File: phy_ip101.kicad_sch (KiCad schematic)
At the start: 48 parts, among them U4 IP101GRI

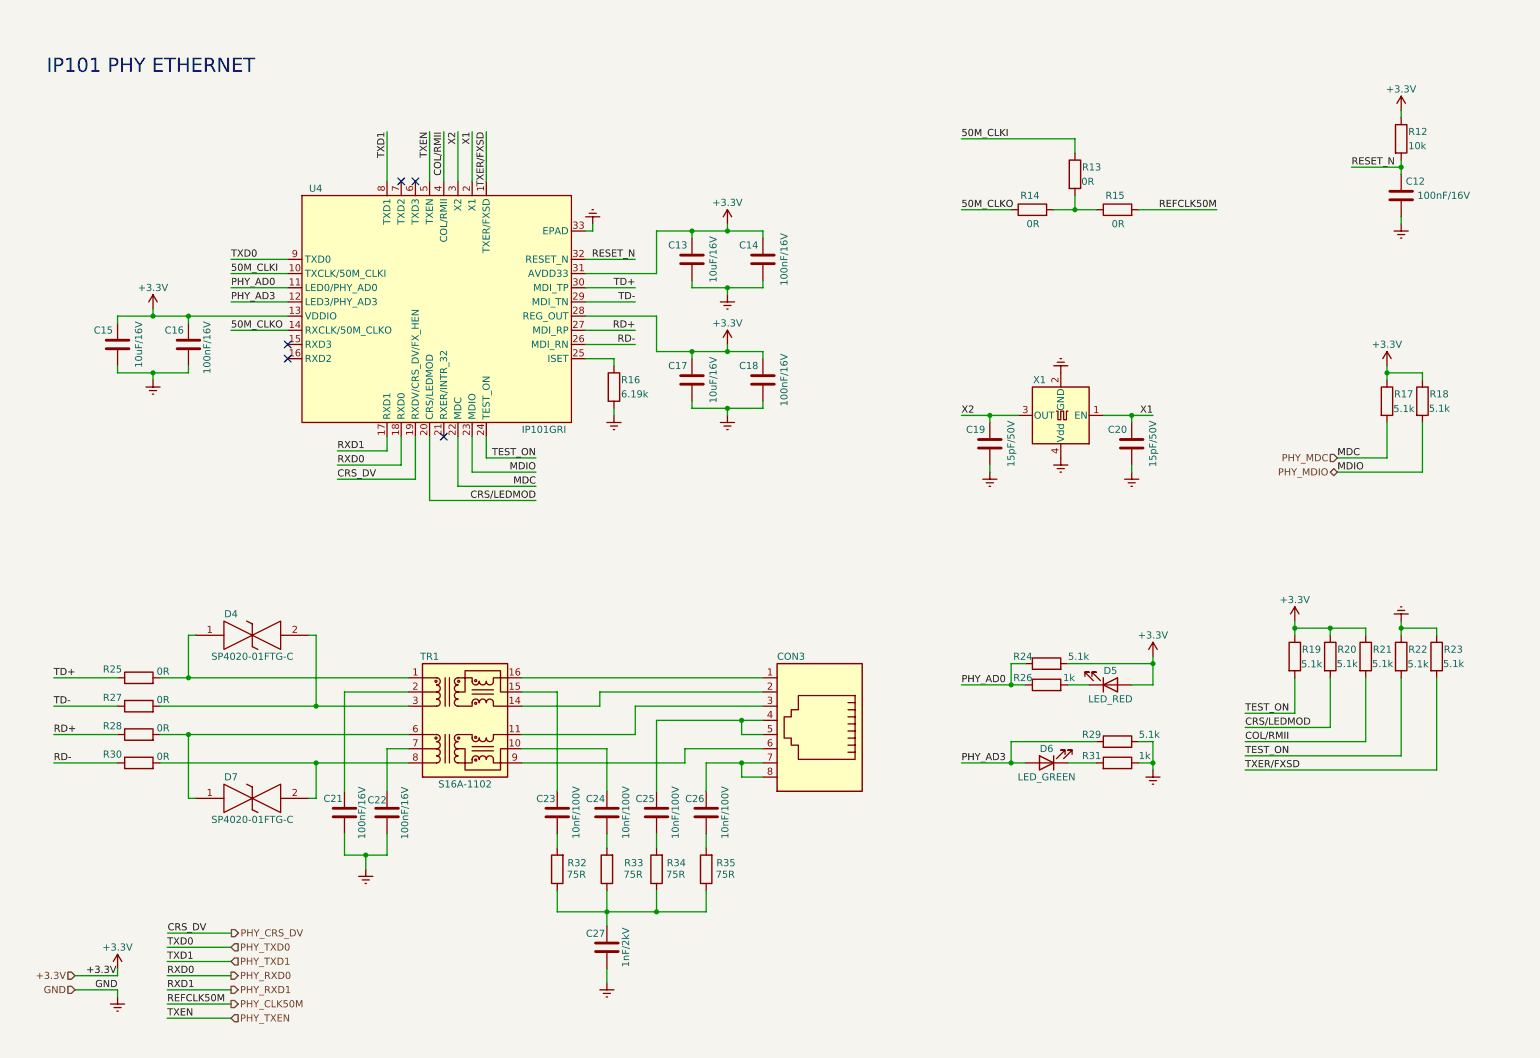
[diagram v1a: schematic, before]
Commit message: Inserido encapsulamento 0603 para os resistores
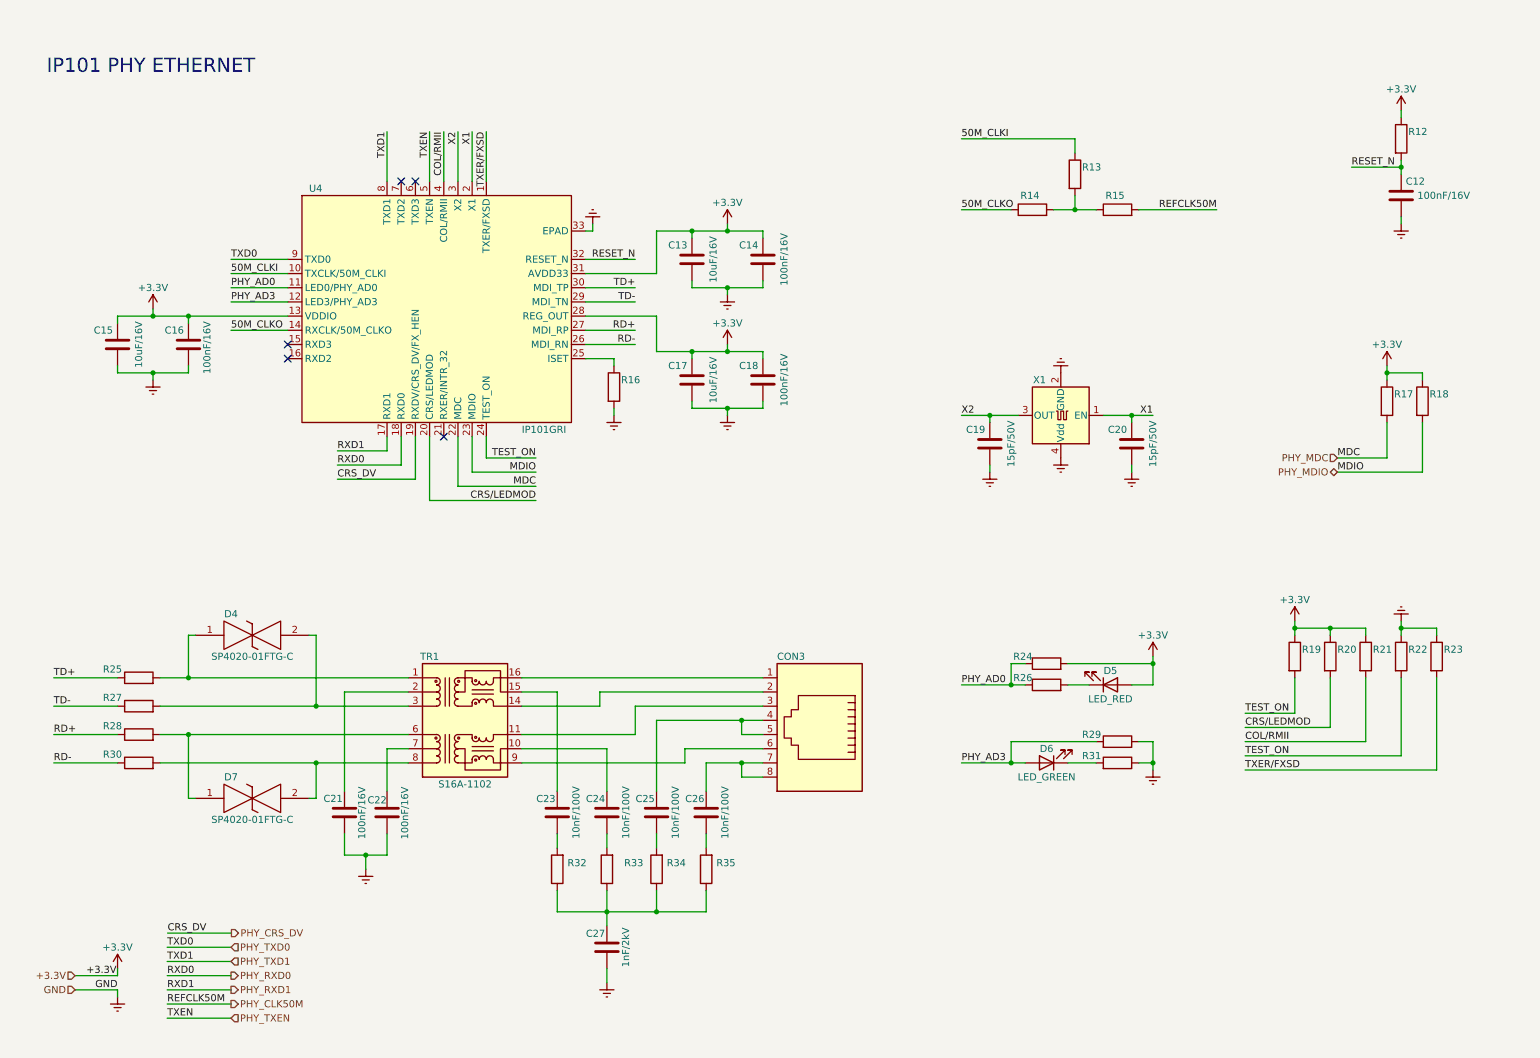
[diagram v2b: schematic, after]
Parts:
- R12: value 10k -> (none); footprint Resistor_SMD:R_0402_1005Metric_Pad0.72x0.64mm_HandSolder -> (none)
- R13, R14, R15, R25, R27, R28, R30: value 0R -> (none); footprint Resistor_SMD:R_0402_1005Metric_Pad0.72x0.64mm_HandSolder -> (none)
- R16: value 6.19k -> (none); footprint Resistor_SMD:R_0402_1005Metric_Pad0.72x0.64mm_HandSolder -> (none)
- R17, R18, R19, R20, R21, R22, R23, R24, R29: value 5.1k -> (none); footprint Resistor_SMD:R_0402_1005Metric_Pad0.72x0.64mm_HandSolder -> (none)
- R26, R31: value 1k -> (none); footprint Resistor_SMD:R_0402_1005Metric_Pad0.72x0.64mm_HandSolder -> (none)
- R32, R33, R34, R35: value 75R -> (none); footprint Resistor_SMD:R_0402_1005Metric_Pad0.72x0.64mm_HandSolder -> (none)

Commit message: Corrigido alguns ERC e adicionado circuito DTR e RI do BG95
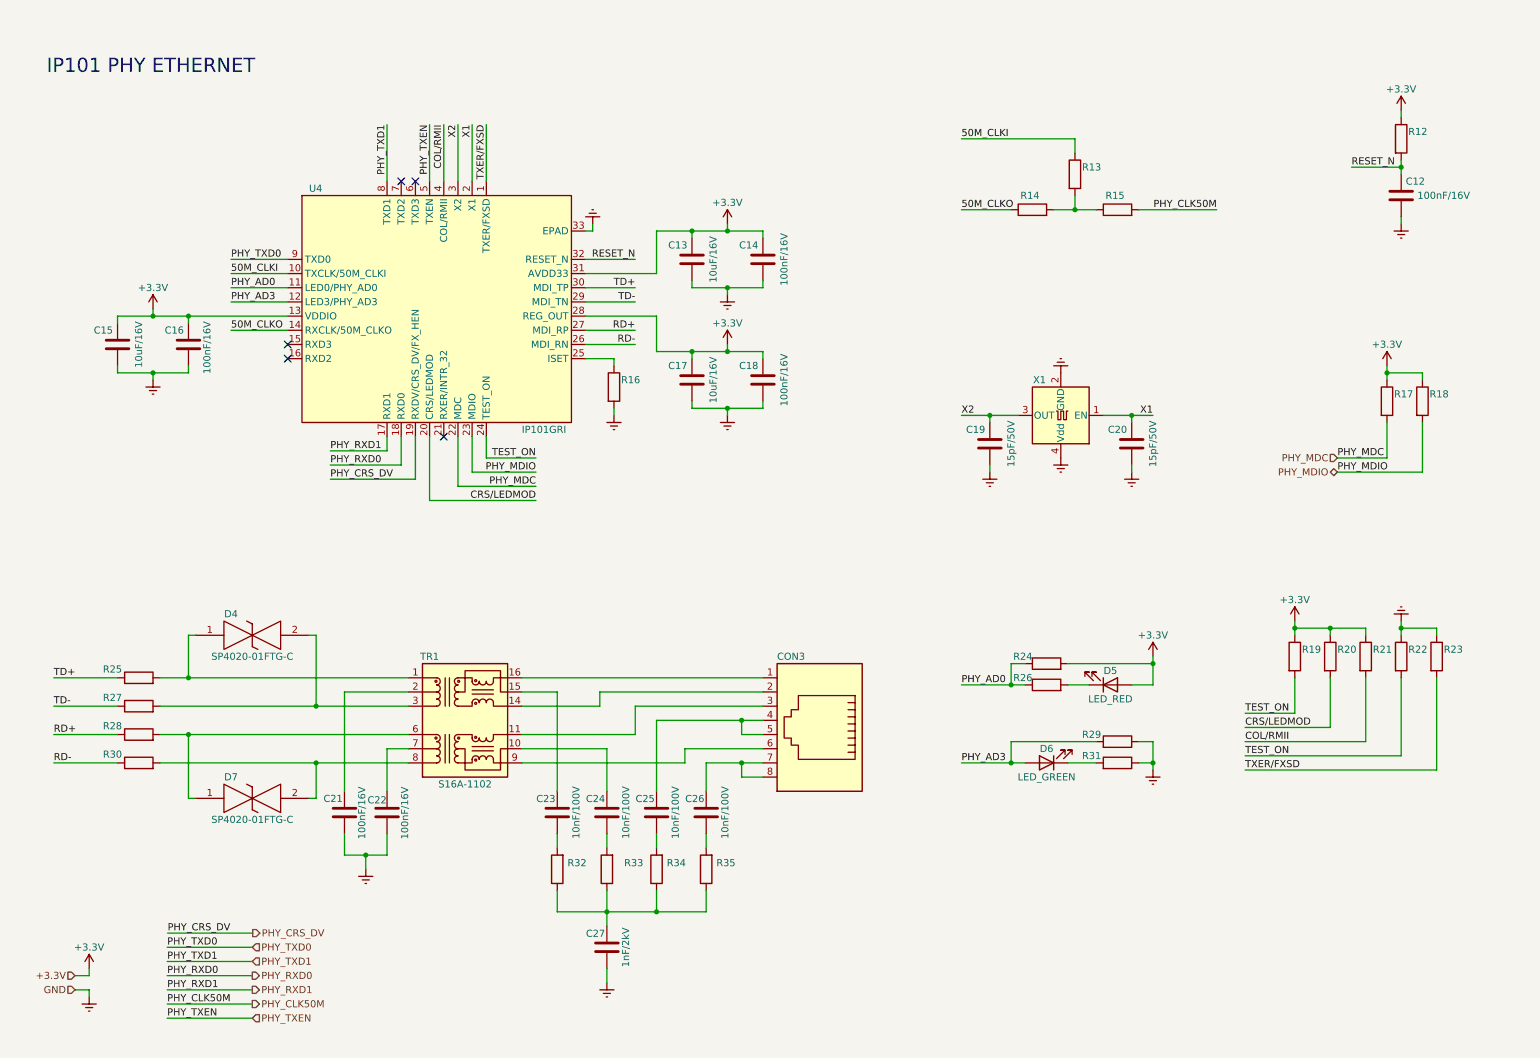
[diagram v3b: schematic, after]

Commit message: Correções de ECR-Electrical Rules Checker
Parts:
- U4: footprint Package_DFN_QFN:QFN-32-1EP_4x4mm_P0.4mm_EP2.9x2.9mm_ThermalVias -> Package_DFN_QFN:HVQFN-32-1EP_5x5mm_P0.5mm_EP3.1x3.1mm_ThermalVias
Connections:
- net GNDREF renamed GND

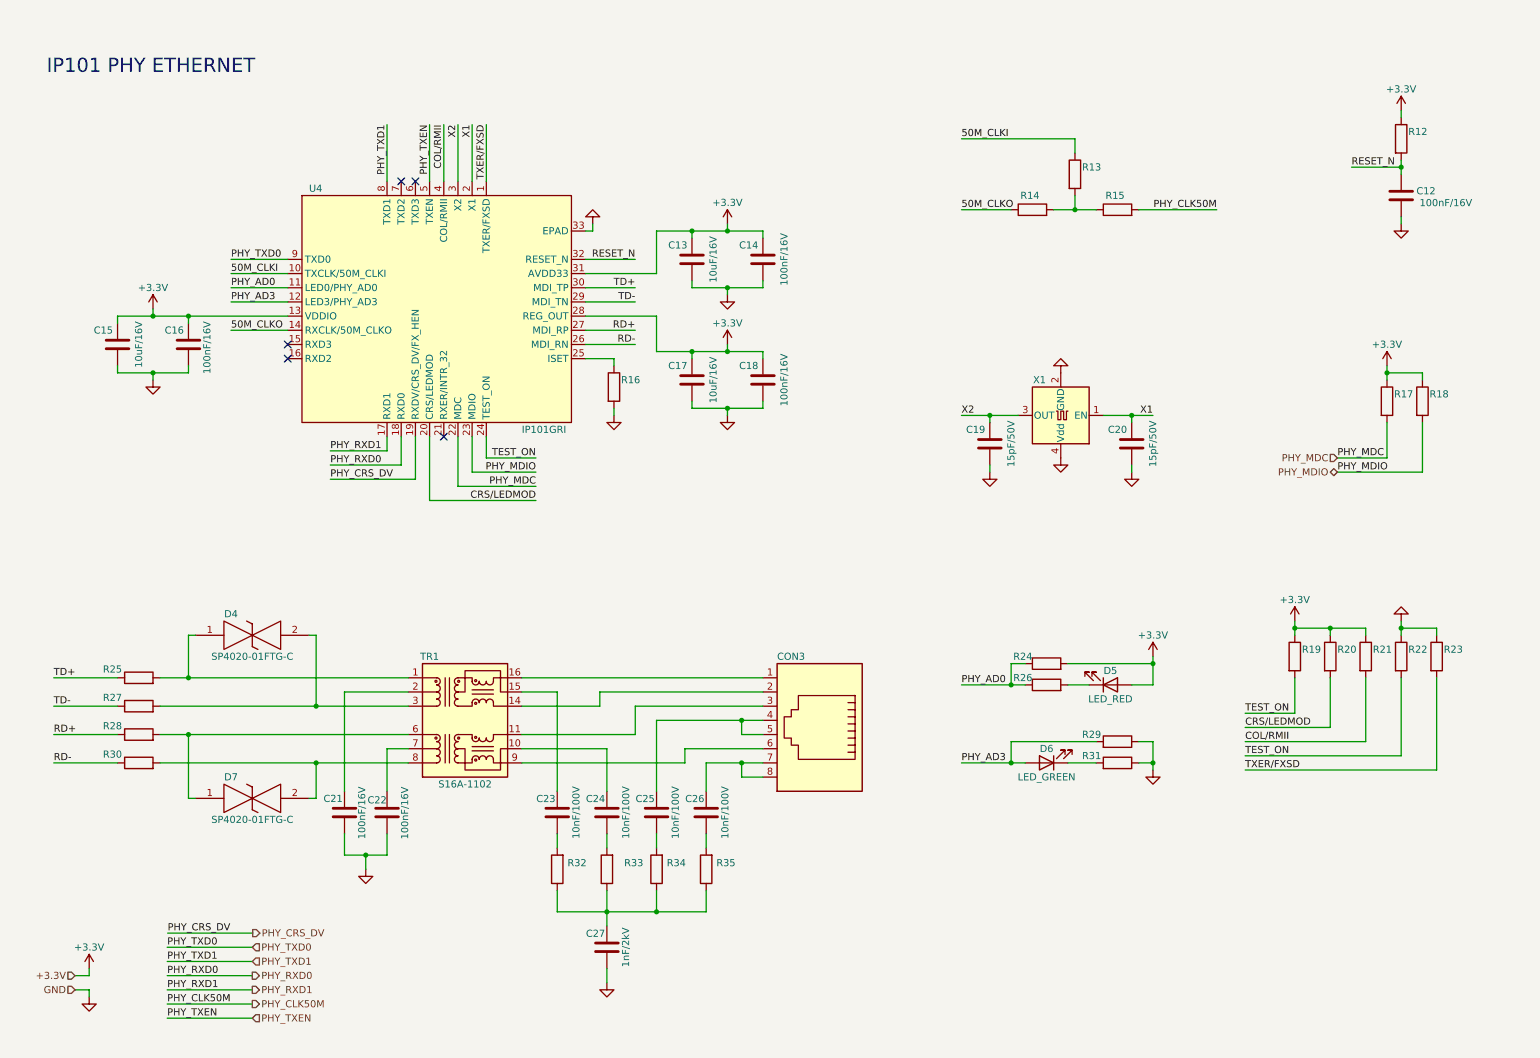
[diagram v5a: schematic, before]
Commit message: Atualização das referências dos componentes
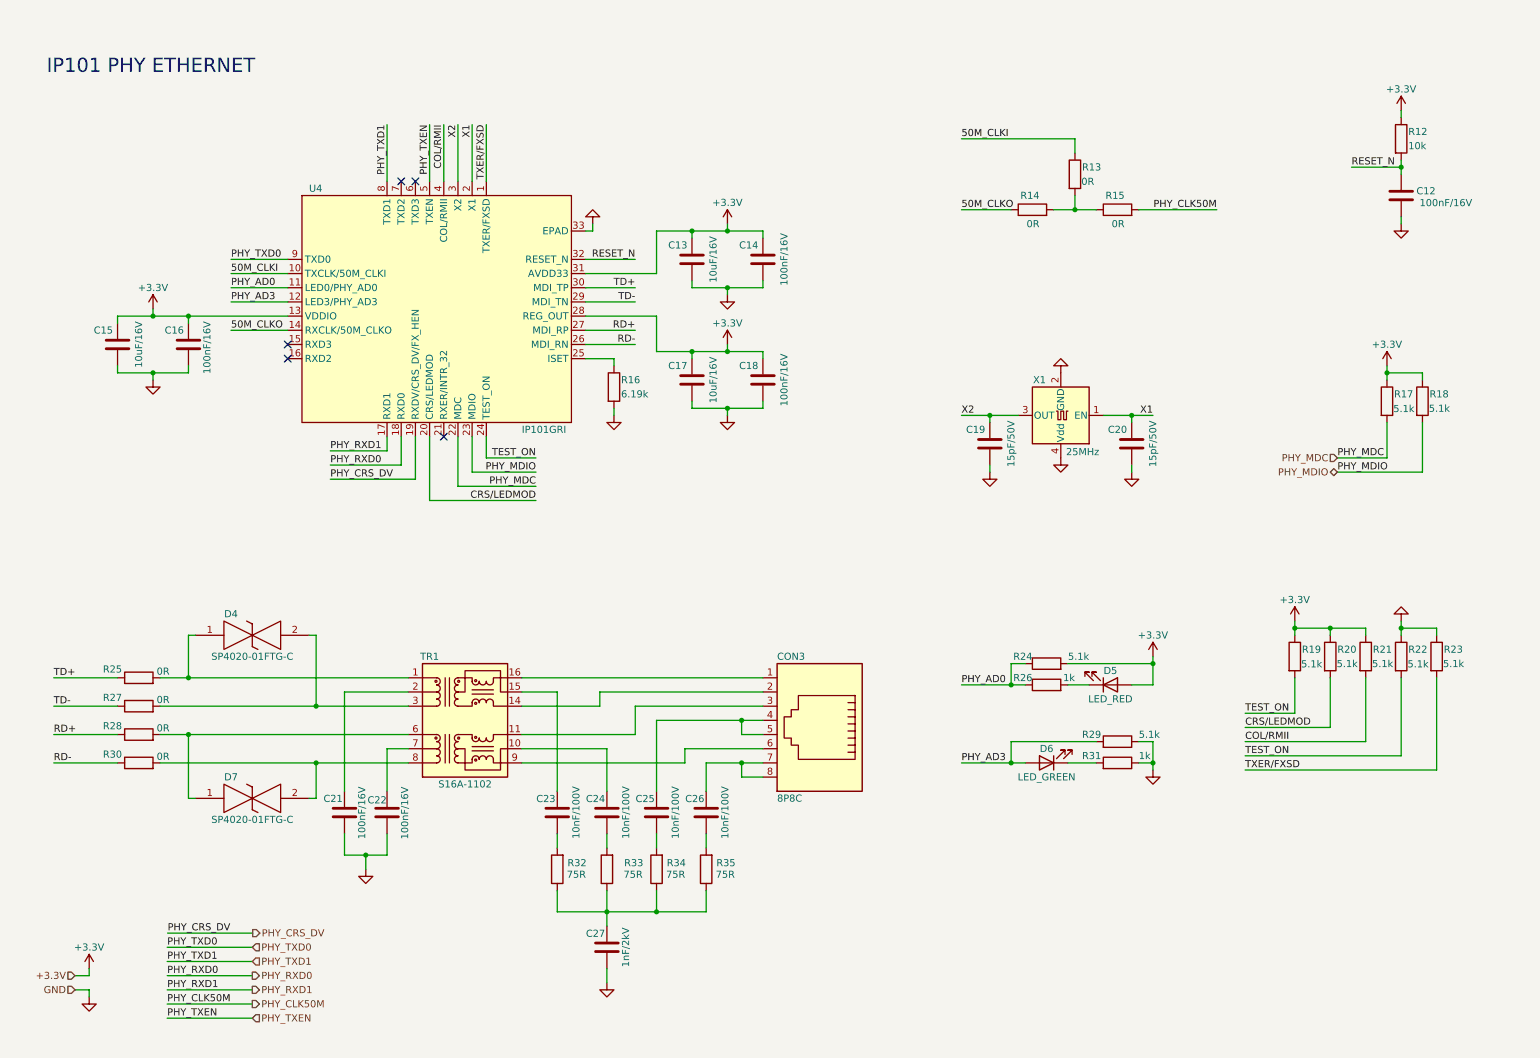
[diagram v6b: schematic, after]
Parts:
- CON3: value (none) -> 8P8C; footprint (none) -> Connector_RJ:RJ45_OST_PJ012-8P8CX_Vertical
- R12: value (none) -> 10k; footprint (none) -> Resistor_SMD:R_0603_1608Metric_Pad0.98x0.95mm_HandSolder
- R13, R14, R15, R25, R27, R28, R30: value (none) -> 0R; footprint (none) -> Resistor_SMD:R_0603_1608Metric_Pad0.98x0.95mm_HandSolder
- R16: value (none) -> 6.19k; footprint (none) -> Resistor_SMD:R_0603_1608Metric_Pad0.98x0.95mm_HandSolder
- R17, R18, R19, R20, R21, R22, R23, R24, R29: value (none) -> 5.1k; footprint (none) -> Resistor_SMD:R_0603_1608Metric_Pad0.98x0.95mm_HandSolder
- R26, R31: value (none) -> 1k; footprint (none) -> Resistor_SMD:R_0603_1608Metric_Pad0.98x0.95mm_HandSolder
- R32, R33, R34, R35: value (none) -> 75R; footprint (none) -> Resistor_SMD:R_0603_1608Metric_Pad0.98x0.95mm_HandSolder
- X1: value (none) -> 25MHz; footprint (none) -> Oscillator:Oscillator_SMD_Abracon_ASE-4Pin_3.2x2.5mm
